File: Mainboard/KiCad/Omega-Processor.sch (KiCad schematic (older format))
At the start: 24 parts, among them J9 PRINTER, U1 Z84C00, U12 ATF16V8B, U24 74HCT273, U27 74HCT175, U33 74AHCT125, U34 74HCT74, U35 74HCT74, U37 74AHCT32, U42 74LS07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

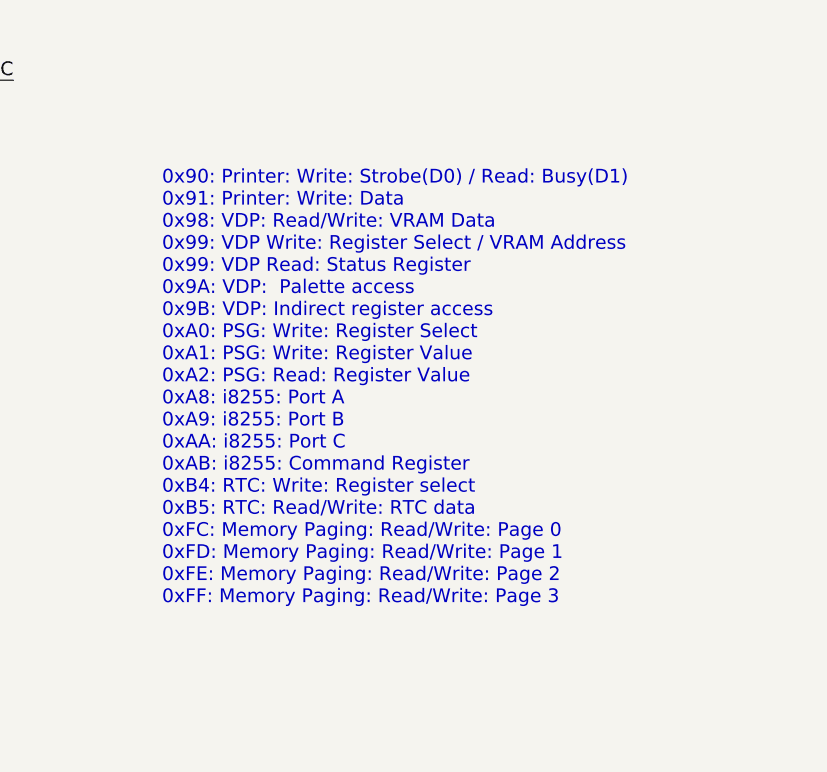
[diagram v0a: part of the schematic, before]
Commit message: Mainboard: Update to version 1.0
Signed-off-by: Sergey Kiselev <skiselev@gmail.com>
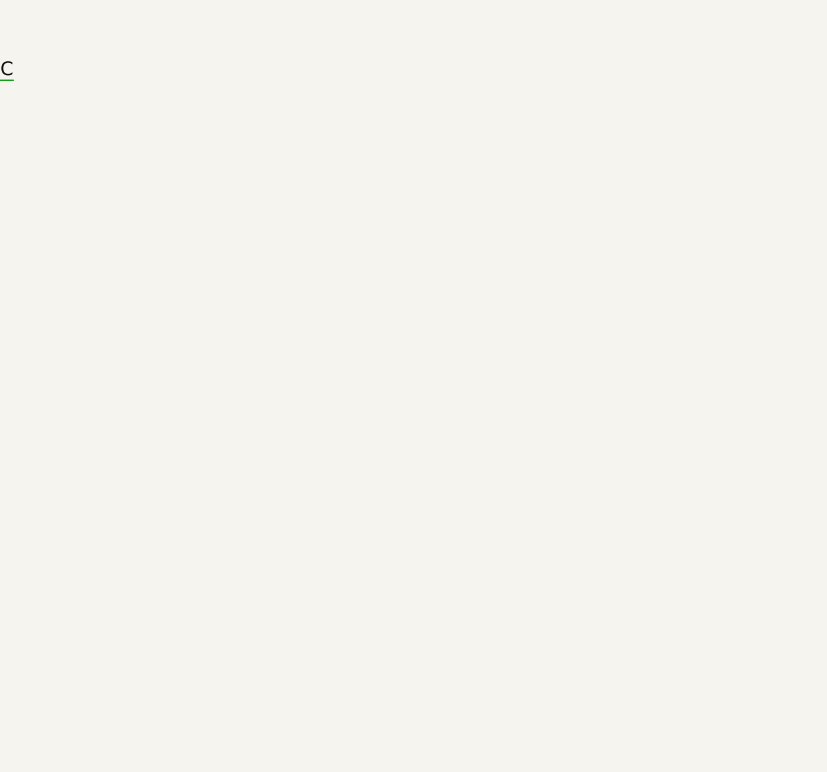
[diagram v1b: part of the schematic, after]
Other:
- note removed: "0x90: Printer: Write: Strobe(D0) / Read: Busy(D1)\n0x91: Printer: Write: Data\n0x98: VDP: Read/Write: VRAM Data\n0x99: VDP Write: Register Select / VRAM Address\n0x99: VDP Read: Status Register\n0x9A: VDP: Palette access\n0x9B: VDP: Indirect register access\n0xA0: PSG: Write: Register Select\n0xA1: PSG: Write: Register Value\n0xA2: PSG: Read: Register Value\n0xA8: i8255: Port A\n0xA9: i8255: Port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"
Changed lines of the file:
@@
 ~RESET
 NoConn ~ 4900 2700
-Text Notes 11650 6600 0    60   ~ 0
-0x90: Printer: Write: Strobe(D0) / Read: Busy(D1)\n0x91: Printer: Write: Data\n0x98: VDP: Read/Write: VRAM Data\n0x99: VDP Write: Register Select / VRAM Address\n0x99: VDP Read: Status Register\n0x9A: VDP:  Palette access\n0x9B: VDP: Indirect register access\n0xA0: PSG: Write: Register Select\n0xA1: PSG: Write: Register Value\n0xA2: PSG: Read: Register Value\n0xA8: i8255: Port A\n0xA9: i8255: Port B\n0xAA: i8255: Port C\n0xAB: i8255: Command Register\n0xB4: RTC: Write: Register select\n0xB5: RTC: Read/Write: RTC data\n0xFC: Memory Paging: Read/Write: Page 0\n0xFD: Memory Paging: Read/Write: Page 1\n0xFE: Memory Paging: Read/Write: Page 2\n0xFF: Memory Paging: Read/Write: Page 3
 $Comp
 L my_components:74LS74 U34

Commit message: Mainboard: Fixed schematic and PCB for v1.1
Signed-off-by: Sergey Kiselev <skiselev@gmail.com>
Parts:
- removed J9: PRINTER, My_Components:Conn_Dsub_DB25F, symbol Connector:DB25_Female
- added J9: PRINTER, My_Components:Conn_Micro_Ribbon_14F, symbol Connector_Generic:Conn_02x07_Top_Bottom
- renumbered R25 to R31
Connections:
- wire segments 297 -> 282
- no-connect marks 26 -> 23
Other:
- moved on the sheet: U27

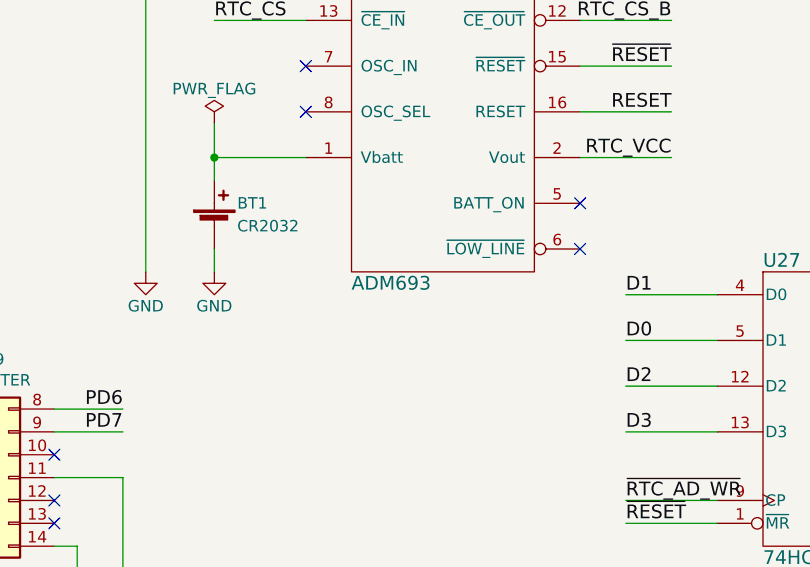
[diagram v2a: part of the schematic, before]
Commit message: Mainboard: Update schematic and PCB layout with latest fixes
Signed-off-by: Sergey Kiselev <skiselev@gmail.com>
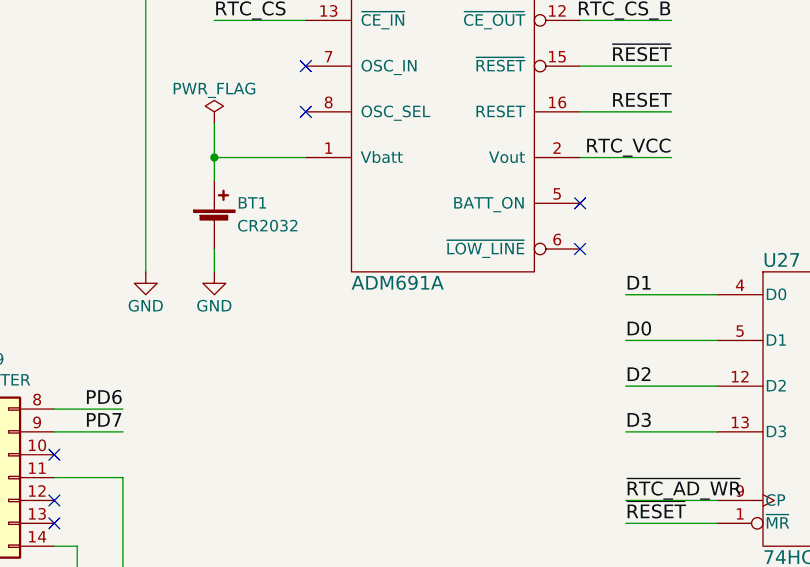
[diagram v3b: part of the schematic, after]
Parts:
- U46: value ADM693 -> ADM691A
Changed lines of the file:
@@
 P 5500 4400
 F 0 "U46" H 5100 5250 60  0000 L CNN
-F 1 "ADM693" H 5100 3550 60  0000 L CNN
+F 1 "ADM691A" H 5100 3550 60  0000 L CNN
 F 2 "My_Components:IC_DIP16_300" H 5500 4600 60  0001 C CNN
 F 3 "" H 5500 4600 60  0000 C CNN

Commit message: Mainboard: Fix some of the issues described in #1
Signed-off-by: Sergey Kiselev <skiselev@gmail.com>
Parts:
- added J13: ~RST~/~NMI, My_Components:Conn_Pin_Header_2x2_2.54mm, symbol Connector_Generic:Conn_02x02_Odd_Even
- renumbered C87 to C85, C89 to C87, C90 to C88, R31 to R29
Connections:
- net GND: now also J13.2 (Pin_2), J13.4 (Pin_4)
- net PRT_BUSY: no longer RR5.3
- net ~BUSREQ: now also RR5.3; no longer RR5.4
- net ~NMI: now also RR5.4, J13.3 (Pin_3); no longer RR5.5
- net ~RESET: now also J13.1 (Pin_1)
- no-connect marks 23 -> 24
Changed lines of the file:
@@
 Text Label 4500 1500 0    60   ~ 0
 ~RFSH
-Text Label 8000 2800 0    60   ~ 0
+Text Label 8000 2700 0    60   ~ 0
 ~NMI
-Text Label 8000 2700 0    60   ~ 0
+Text Label 8000 2600 0    60   ~ 0
 ~BUSREQ
 Text Label 4500 2100 0    60   ~ 0
@@
 $EndComp
 $Comp
-L Device:C C87
+L Device:C C85
 U 1 1 5BF85069
 P 7750 3800
-F 0 "C87" H 7775 3900 50  0000 L CNN
+F 0 "C85" H 7775 3900 50  0000 L CNN
 F 1 "68pF" H 7775 3700 50  0000 L CNN
 F 2 "My_Components:Cap_Cer_508" H 7788 3650 50  0001 C CNN
@@
 $EndComp
 $Comp
-L Device:C C90
+L Device:C C88
 U 1 1 5BF850EC
 P 7750 4300
-F 0 "C90" H 7775 4400 50  0000 L CNN
+F 0 "C88" H 7775 4400 50  0000 L CNN
 F 1 "33pF" H 7775 4200 50  0000 L CNN
 F 2 "My_Components:Cap_Cer_508" H 7788 4150 50  0001 C CNN
@@
 $EndComp
 $Comp
-L Device:C C89
+L Device:C C87
 U 1 1 5BF8514D
 P 7750 4800
-F 0 "C89" H 7775 4900 50  0000 L CNN
+F 0 "C87" H 7775 4900 50  0000 L CNN
 F 1 "33pF" H 7775 4700 50  0000 L CNN
 F 2 "My_Components:Cap_Cer_508" H 7788 4650 50  0001 C CNN
@@
 	8500 2500 8000 2500
 Wire Wire Line
-	8500 2600 8000 2600
-Wire Wire Line
 	4900 1500 4500 1500
 Wire Wire Line
-	8000 2800 8500 2800
+	8000 2700 8500 2700
 Wire Wire Line
 	8000 2900 8500 2900
@@
 	8000 3300 8500 3300
 Wire Wire Line
-	8000 2700 8500 2700
+	8000 2600 8500 2600
 Wire Wire Line
 	4300 2100 4900 2100
@@
 Connection ~ 3900 2900
 $Comp
-L Device:R R31
+L Device:R R29
 U 1 1 5C039811
 P 900 1750
-F 0 "R31" V 980 1750 50  0000 C CNN
+F 0 "R29" V 980 1750 50  0000 C CNN
 F 1 "1k" V 900 1750 50  0000 C CNN
 F 2 "My_Components:Res_762" V 830 1750 50  0001 C CNN
@@
 Wire Wire Line
 	7700 5300 8700 5300
-Text Label 8000 2600 0    60   ~ 0
-PRT_BUSY
 NoConn ~ 8500 3100
 $Comp
@@
 Wire Wire Line
 	1900 7400 4100 7400
+Text Label 10200 3300 0    60   ~ 0
+PRT_BUSY
+Wire Wire Line
+	10600 3300 10200 3300
+Text HLabel 10600 3300 2    60   Output ~ 0
+PRT_BUSY
+NoConn ~ 8500 2800
+$Comp
+L Connector_Generic:Conn_02x02_Odd_Even J13
+U 1 1 5F89FB61
+P 5200 5800
+F 0 "J13" H 5250 6029 50  0000 C CNN
+F 1 "~RST~/~NMI" H 5250 5931 50  0000 C CNN
+F 2 "My_Components:Conn_Pin_Header_2x2_2.54mm" H 5200 5800 50  0001 C CNN
+F 3 "~" H 5200 5800 50  0001 C CNN
+	1    5200 5800
+	1    0    0    -1
+$EndComp
+Wire Wire Line
+	5500 5800 5600 5800
+Wire Wire Line
+	5600 5800 5600 5900
+Wire Wire Line
+	5500 5900 5600 5900
+Connection ~ 5600 5900
+Wire Wire Line
+	5600 5900 5600 6000
+Wire Wire Line
+	5000 5800 4600 5800
+Wire Wire Line
+	5000 5900 4600 5900
+Text Label 4600 5800 0    60   ~ 0
+~RESET
+Text Label 4600 5900 0    60   ~ 0
+~NMI
+$Comp
+L power:GND #PWR0155
+U 1 1 5F907B82
+P 5600 6000
+F 0 "#PWR0155" H 5600 5750 50  0001 C CNN
+F 1 "GND" H 5600 5850 50  0000 C CNN
+F 2 "" H 5600 6000 50  0001 C CNN
+F 3 "" H 5600 6000 50  0001 C CNN
+	1    5600 6000
+	1    0    0    -1
+$EndComp
 $EndSCHEMATC

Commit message: Mainboard: Swap slots, use trmp cap for RTC, add color bus
Signed-off-by: Sergey Kiselev <skiselev@gmail.com>
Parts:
- C88: renamed from C85; value 68pF -> 30pF; footprint My_Components:Cap_Cer_508 -> My_Components:C_Trim_Murata; symbol Device:C -> Device:CTRIM
- renumbered C87 to C86, C88 to C87
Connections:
- net GND: now also U12.10 (GND)
- net VCC: now also U12.20 (VCC)
- net ~BUSDIR1: now also RR5.7; no longer RR5.6
- net ~BUSDIR2: now also RR5.6; no longer RR5.7
- net at C88.2, U5.16 (OSCIN): now also Y2.1; no longer Y2.2
- net at C87.2, R5.2: now also Y2.2; no longer Y2.1
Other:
- moved on the sheet: RR1, RR5, U12

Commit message: Add files for version 1.3eu from Jordi Solis
Signed-off-by: Sergey Kiselev <skiselev@gmail.com>
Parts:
- RR1, RR5: symbol my_components:RR9 -> Omega-Mainboard-rescue:RR9-my_components
- U1: symbol my_components:Z84C00 -> Omega-Mainboard-rescue:Z84C00-my_components
- U12: symbol my_components:ATF16V8B -> Omega-Mainboard-rescue:ATF16V8B-my_components
- U24: symbol my_components:74LS273 -> Omega-Mainboard-rescue:74LS273-my_components
- U27: symbol my_components:74LS175 -> Omega-Mainboard-rescue:74LS175-my_components
- U33: symbol my_components:74LS125 -> Omega-Mainboard-rescue:74LS125-my_components
- U34, U35: symbol my_components:74LS74 -> Omega-Mainboard-rescue:74LS74-my_components
- U37: symbol my_components:74LS32 -> Omega-Mainboard-rescue:74LS32-my_components
- U42: symbol my_components:74LS07 -> Omega-Mainboard-rescue:74LS07-my_components
- U45: symbol my_components:74LS00 -> Omega-Mainboard-rescue:74LS00-my_components
- U46: symbol my_components:ADM693 -> Omega-Mainboard-rescue:ADM693-my_components
- U5: symbol my_components:RP5C01 -> Omega-Mainboard-rescue:RP5C01-my_components
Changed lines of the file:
@@
 EESchema Schematic File Version 4
 LIBS:Omega-Mainboard-cache
-EELAYER 29 0
+EELAYER 30 0
 EELAYER END
 $Descr A4 11693 8268
@@
 $EndDescr
 $Comp
-L my_components:Z84C00 U1
+L Omega-Mainboard-rescue:Z84C00-my_components U1
 U 1 1 5A3B4790
 P 5500 2000
@@
 NoConn ~ 4900 2700
 $Comp
-L my_components:74LS74 U34
+L Omega-Mainboard-rescue:74LS74-my_components U34
 U 1 1 5BEC65BD
 P 1800 1500
@@
 $EndComp
 $Comp
-L my_components:74LS74 U34
+L Omega-Mainboard-rescue:74LS74-my_components U34
 U 2 1 5BEC6693
 P 3700 1500
@@
 ~WR
 $Comp
-L my_components:RR9 RR5
+L Omega-Mainboard-rescue:RR9-my_components RR5
 U 1 1 5BECD787
 P 8800 3050
@@
 D7
 $Comp
-L my_components:RP5C01 U5
+L Omega-Mainboard-rescue:RP5C01-my_components U5
 U 1 1 5A4D551B
 P 9300 5200
@@
 A6
 $Comp
-L my_components:ATF16V8B U12
+L Omega-Mainboard-rescue:ATF16V8B-my_components U12
 U 1 1 5BF764B1
 P 7800 1550
@@
 D3
 $Comp
-L my_components:74LS175 U27
+L Omega-Mainboard-rescue:74LS175-my_components U27
 U 1 1 5BF7A32E
 P 7200 5800
@@
 ~RTC_AD_WR
 $Comp
-L my_components:RR9 RR1
+L Omega-Mainboard-rescue:RR9-my_components RR1
 U 1 1 5BF3C9E5
 P 7600 3050
@@
 D7
 $Comp
-L my_components:ADM693 U46
+L Omega-Mainboard-rescue:ADM693-my_components U46
 U 1 1 5BF4A892
 P 5500 4400
@@
 $EndComp
 $Comp
-L my_components:74LS273 U24
+L Omega-Mainboard-rescue:74LS273-my_components U24
 U 1 1 5BFFD3D6
 P 1800 6200
@@
 ~RESET
 $Comp
-L my_components:74LS74 U35
+L Omega-Mainboard-rescue:74LS74-my_components U35
 U 1 1 5BFFF140
 P 1800 4900
@@
 PRT_BUSY
 $Comp
-L my_components:74LS125 U33
+L Omega-Mainboard-rescue:74LS125-my_components U33
 U 1 1 5C0029D9
 P 1600 7400
@@
 D1
 $Comp
-L my_components:74LS32 U37
+L Omega-Mainboard-rescue:74LS32-my_components U37
 U 3 2 5C0035A9
 P 1700 3650
@@
 	1300 3700 1300 4100
 $Comp
-L my_components:74LS32 U37
+L Omega-Mainboard-rescue:74LS32-my_components U37
 U 2 2 5C003633
 P 1700 4150
@@
 $EndComp
 $Comp
-L my_components:74LS125 U33
+L Omega-Mainboard-rescue:74LS125-my_components U33
 U 3 1 5C0368DF
 P 5600 7000
@@
 	9100 2800 9500 2800
 $Comp
-L my_components:74LS00 U45
+L Omega-Mainboard-rescue:74LS00-my_components U45
 U 3 1 5C04F04D
 P 3100 2250
@@
 $EndComp
 $Comp
-L my_components:74LS00 U45
+L Omega-Mainboard-rescue:74LS00-my_components U45
 U 4 2 5C04F134
 P 2200 2250
@@
 Connection ~ 2700 2250
 $Comp
-L my_components:74LS07 U42
+L Omega-Mainboard-rescue:74LS07-my_components U42
 U 4 1 5C14362A
 P 3100 2900
@@
 $EndComp
 $Comp
-L my_components:74LS125 U33
+L Omega-Mainboard-rescue:74LS125-my_components U33
 U 2 1 5C1540B4
 P 4800 7000
@@
 $EndComp
 $Comp
-L my_components:74LS125 U33
+L Omega-Mainboard-rescue:74LS125-my_components U33
 U 4 1 5C1543B6
 P 6400 7000

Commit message: Version 1.4: Add cut-out for the right angle slot connector. Add optional jumpers to limit memory mapper address range
Signed-off-by: Sergey Kiselev <skiselev@gmail.com>
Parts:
- RR1, RR5: symbol Omega-Mainboard-rescue:RR9-my_components -> my_components:RR9
- U1: symbol Omega-Mainboard-rescue:Z84C00-my_components -> my_components:Z84C00
- U12: symbol Omega-Mainboard-rescue:ATF16V8B-my_components -> my_components:ATF16V8B
- U24: symbol Omega-Mainboard-rescue:74LS273-my_components -> my_components:74LS273
- U27: symbol Omega-Mainboard-rescue:74LS175-my_components -> my_components:74LS175
- U33: symbol Omega-Mainboard-rescue:74LS125-my_components -> my_components:74LS125
- U34, U35: symbol Omega-Mainboard-rescue:74LS74-my_components -> my_components:74LS74
- U37: symbol Omega-Mainboard-rescue:74LS32-my_components -> my_components:74LS32
- U42: symbol Omega-Mainboard-rescue:74LS07-my_components -> my_components:74LS07
- U45: symbol Omega-Mainboard-rescue:74LS00-my_components -> my_components:74LS00
- U5: symbol Omega-Mainboard-rescue:RP5C01-my_components -> my_components:RP5C01
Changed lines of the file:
@@
 EESchema Schematic File Version 4
-LIBS:Omega-Mainboard-cache
 EELAYER 30 0
 EELAYER END
@@
 $EndDescr
 $Comp
-L Omega-Mainboard-rescue:Z84C00-my_components U1
+L my_components:Z84C00 U1
 U 1 1 5A3B4790
 P 5500 2000
@@
 NoConn ~ 4900 2700
 $Comp
-L Omega-Mainboard-rescue:74LS74-my_components U34
+L my_components:74LS74 U34
 U 1 1 5BEC65BD
 P 1800 1500
@@
 $EndComp
 $Comp
-L Omega-Mainboard-rescue:74LS74-my_components U34
+L my_components:74LS74 U34
 U 2 1 5BEC6693
 P 3700 1500
@@
 ~WR
 $Comp
-L Omega-Mainboard-rescue:RR9-my_components RR5
+L my_components:RR9 RR5
 U 1 1 5BECD787
 P 8800 3050
@@
 D7
 $Comp
-L Omega-Mainboard-rescue:RP5C01-my_components U5
+L my_components:RP5C01 U5
 U 1 1 5A4D551B
 P 9300 5200
@@
 A6
 $Comp
-L Omega-Mainboard-rescue:ATF16V8B-my_components U12
+L my_components:ATF16V8B U12
 U 1 1 5BF764B1
 P 7800 1550
@@
 D3
 $Comp
-L Omega-Mainboard-rescue:74LS175-my_components U27
+L my_components:74LS175 U27
 U 1 1 5BF7A32E
 P 7200 5800
@@
 ~RTC_AD_WR
 $Comp
-L Omega-Mainboard-rescue:RR9-my_components RR1
+L my_components:RR9 RR1
 U 1 1 5BF3C9E5
 P 7600 3050
@@
 $EndComp
 $Comp
-L Omega-Mainboard-rescue:74LS273-my_components U24
+L my_components:74LS273 U24
 U 1 1 5BFFD3D6
 P 1800 6200
@@
 ~RESET
 $Comp
-L Omega-Mainboard-rescue:74LS74-my_components U35
+L my_components:74LS74 U35
 U 1 1 5BFFF140
 P 1800 4900
@@
 PRT_BUSY
 $Comp
-L Omega-Mainboard-rescue:74LS125-my_components U33
+L my_components:74LS125 U33
 U 1 1 5C0029D9
 P 1600 7400
@@
 D1
 $Comp
-L Omega-Mainboard-rescue:74LS32-my_components U37
+L my_components:74LS32 U37
 U 3 2 5C0035A9
 P 1700 3650
@@
 	1300 3700 1300 4100
 $Comp
-L Omega-Mainboard-rescue:74LS32-my_components U37
+L my_components:74LS32 U37
 U 2 2 5C003633
 P 1700 4150
@@
 $EndComp
 $Comp
-L Omega-Mainboard-rescue:74LS125-my_components U33
+L my_components:74LS125 U33
 U 3 1 5C0368DF
 P 5600 7000
@@
 	9100 2800 9500 2800
 $Comp
-L Omega-Mainboard-rescue:74LS00-my_components U45
+L my_components:74LS00 U45
 U 3 1 5C04F04D
 P 3100 2250
@@
 $EndComp
 $Comp
-L Omega-Mainboard-rescue:74LS00-my_components U45
+L my_components:74LS00 U45
 U 4 2 5C04F134
 P 2200 2250
@@
 Connection ~ 2700 2250
 $Comp
-L Omega-Mainboard-rescue:74LS07-my_components U42
+L my_components:74LS07 U42
 U 4 1 5C14362A
 P 3100 2900
@@
 $EndComp
 $Comp
-L Omega-Mainboard-rescue:74LS125-my_components U33
+L my_components:74LS125 U33
 U 2 1 5C1540B4
 P 4800 7000
@@
 $EndComp
 $Comp
-L Omega-Mainboard-rescue:74LS125-my_components U33
+L my_components:74LS125 U33
 U 4 1 5C1543B6
 P 6400 7000

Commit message: Fix issue #56, where joystick A trigger 2 was swapped with joystick B trigger 1
Signed-off-by: Sergey Kiselev <skiselev@gmail.com>
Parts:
- U1: symbol my_components:Z84C00 -> my_components:Z84C00-Old-Hidden_Power
- U46: symbol Omega-Mainboard-rescue:ADM693-my_components -> my_components:MAX691-Hidden_Power
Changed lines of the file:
@@
 Comment4 ""
 $EndDescr
-$Comp
-L my_components:Z84C00 U1
-U 1 1 5A3B4790
-P 5500 2000
-F 0 "U1" H 5100 3350 60  0000 L CNN
-F 1 "Z84C00" H 5100 650 60  0000 L CNN
-F 2 "My_Components:IC_DIP40_600" H 5500 2000 60  0001 C CNN
-F 3 "" H 5500 2000 60  0000 C CNN
-	1    5500 2000
-	1    0    0    -1
-$EndComp
 Text Label 4500 2400 0    60   ~ 0
 ~RESET
@@
 D7
 $Comp
-L Omega-Mainboard-rescue:ADM693-my_components U46
+L my_components:MAX691-Hidden_Power U46
 U 1 1 5BF4A892
-P 5500 4400
-F 0 "U46" H 5100 5250 60  0000 L CNN
+P 5500 4500
+F 0 "U46" H 5100 5450 60  0000 L CNN
 F 1 "ADM691A" H 5100 3550 60  0000 L CNN
-F 2 "My_Components:IC_DIP16_300" H 5500 4600 60  0001 C CNN
-F 3 "" H 5500 4600 60  0000 C CNN
-	1    5500 4400
+F 2 "My_Components:IC_DIP16_300" H 5500 4700 60  0001 C CNN
+F 3 "" H 5500 4700 60  0000 C CNN
+	1    5500 4500
 	1    0    0    -1
 $EndComp
@@
 	0    -1   1    0
 $EndComp
+$Comp
+L my_components:Z84C00-Old-Hidden_Power U1
+U 1 1 5A3B4790
+P 5500 2000
+F 0 "U1" H 5100 3350 60  0000 L CNN
+F 1 "Z84C00" H 5100 650 60  0000 L CNN
+F 2 "My_Components:IC_DIP40_600" H 5500 2000 60  0001 C CNN
+F 3 "" H 5500 2000 60  0000 C CNN
+	1    5500 2000
+	1    0    0    -1
+$EndComp
 $EndSCHEMATC
